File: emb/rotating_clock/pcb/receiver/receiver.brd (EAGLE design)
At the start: 100 x 80 mm, 23 parts, among them IC1 A1321LH, IC2 A1321LH, IC3 A1321LH, IC4 LM358D, IC5 LM358D

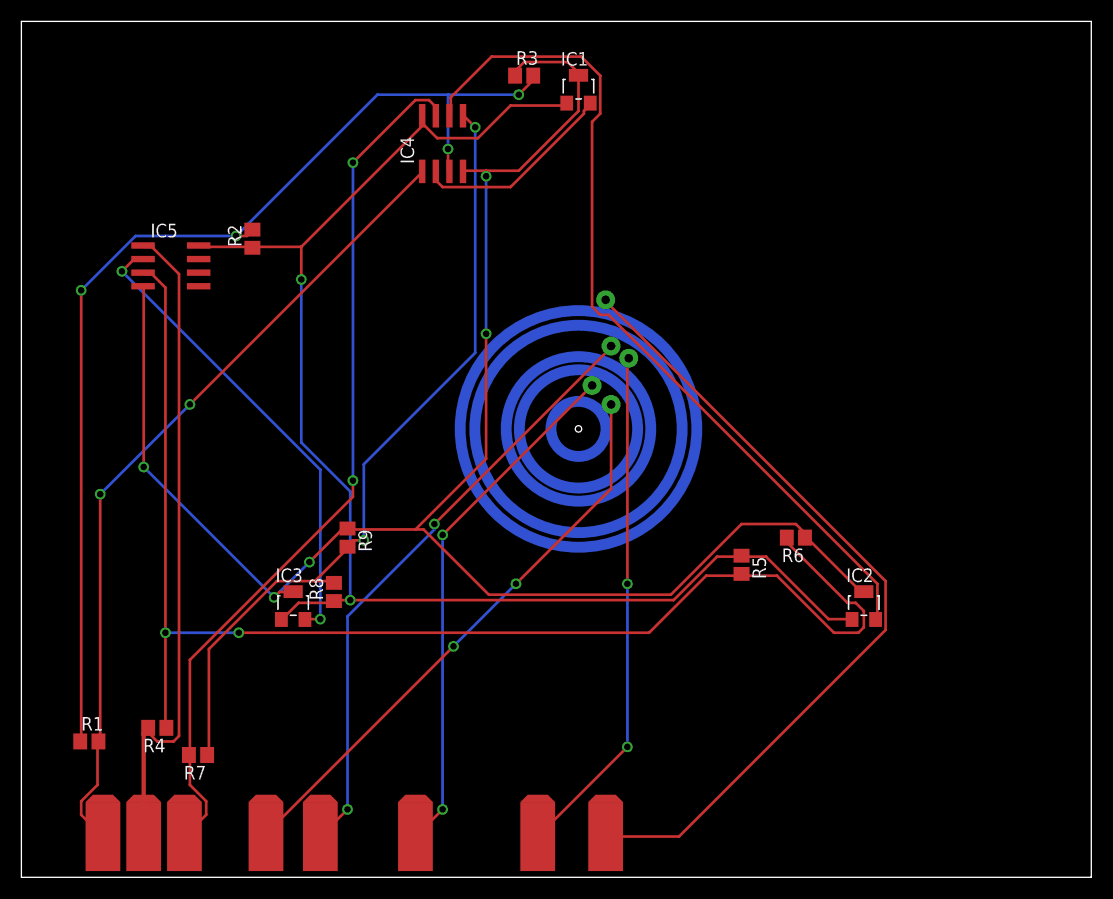
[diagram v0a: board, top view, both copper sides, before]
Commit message: made bot board smaller
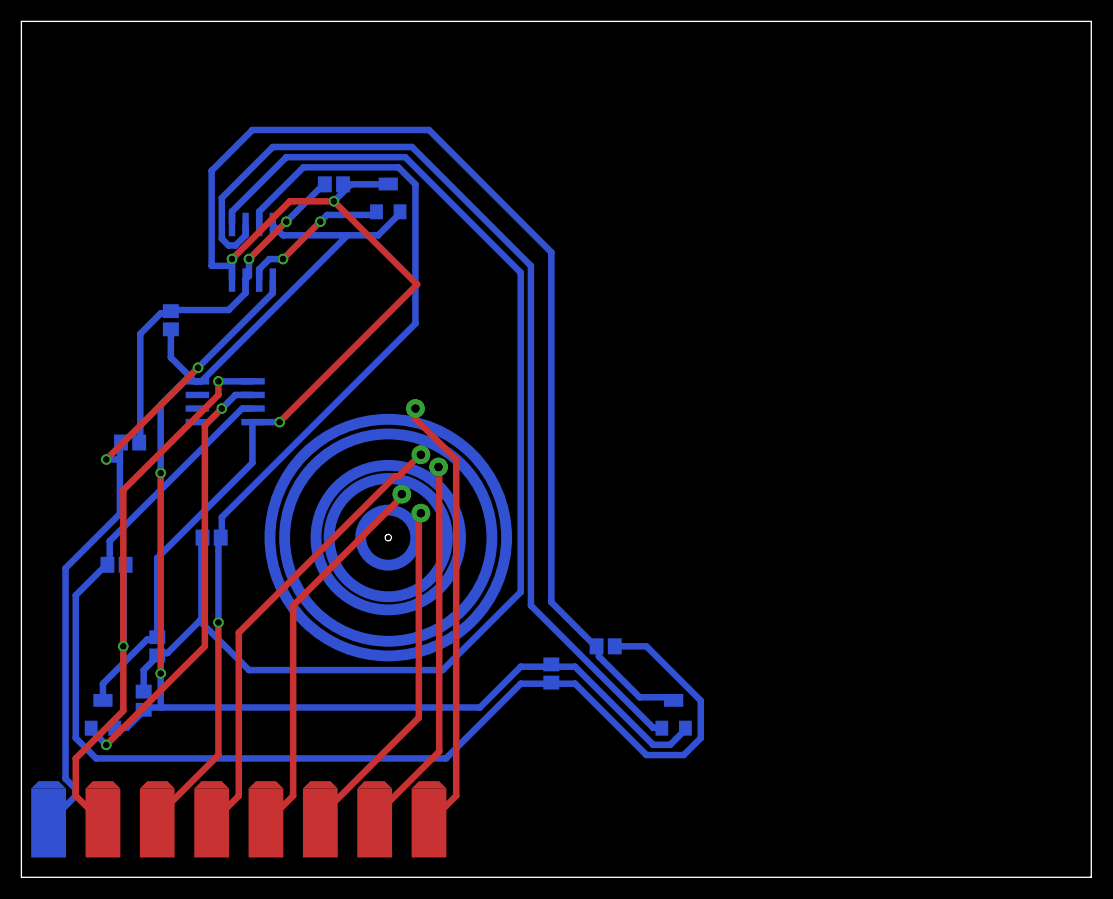
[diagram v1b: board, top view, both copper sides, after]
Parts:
- moved R1 28.2 mm to (10.2, 40.6), flipped to the bottom
- moved R3 20.5 mm to (29.2, 64.8), flipped to the bottom
- moved IC1 20.5 mm to (34.3, 63.5), flipped to the bottom
- moved R5 20.5 mm to (49.5, 19.1), flipped to the bottom
- moved R6 20.5 mm to (54.6, 21.6), flipped to the bottom
- moved R8 20.5 mm to (11.4, 16.5), flipped to the bottom
- moved R9 20.5 mm to (12.7, 21.6), flipped to the bottom
- moved U$1 20.5 mm to (34.3, 31.8)
- moved IC3 20.5 mm to (7.62, 15.2), flipped to the bottom
- moved IC4 20.5 mm to (21.6, 58.4), flipped to the bottom
- moved IC2 20.5 mm to (61.0, 15.2), flipped to the bottom
- moved R7 20.4 mm to (17.8, 31.8), flipped to the bottom
- moved U$7 16.6 mm to (38.1, 5.08)
- moved R4 15.7 mm to (8.89, 29.2), flipped to the bottom
- moved U$5 15.3 mm to (33.0, 5.08)
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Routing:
- net N$1: track 102.2 -> 35.2 mm, vias 4 -> 2
- net N$7: track 75.4 -> 116.8 mm, vias 2 -> 0
- net N$12: track 75.9 -> 41.4 mm
- net N$14: track 53.7 -> 32.9 mm, vias 2 -> 0
- net GND: track 162.4 -> 181.8 mm, vias 5 -> 3
- net N$11: track 57.1 -> 42.7 mm, vias 2 -> 0
- net N$13: track 49.0 -> 36.0 mm, vias 2 -> 0
- net N$2: track 76.3 -> 63.7 mm
- net N$10: track 48.3 -> 35.8 mm, vias 2 -> 0
- net N$9: track 80.8 -> 91.9 mm
- net N$4: track 125.9 -> 117.7 mm, vias 2 -> 0
- net N$8: track 82.1 -> 88.1 mm, vias 2 -> 1
- net +3V3: track 136.2 -> 131.0 mm
- net N$3: track 19.0 -> 14.2 mm, vias 0 -> 2
- net N$5: track 61.8 -> 58.9 mm, vias 0 -> 2
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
